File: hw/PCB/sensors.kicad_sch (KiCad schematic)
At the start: 1 part, among them U6 RM3100

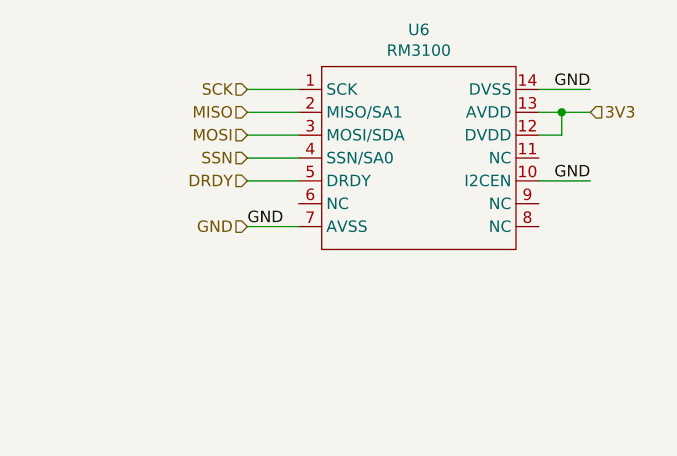
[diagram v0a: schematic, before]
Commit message: Modified the design of the femto-satellite. Now it is smaller an it has a temperature sensor to calibrate the magnetometer.
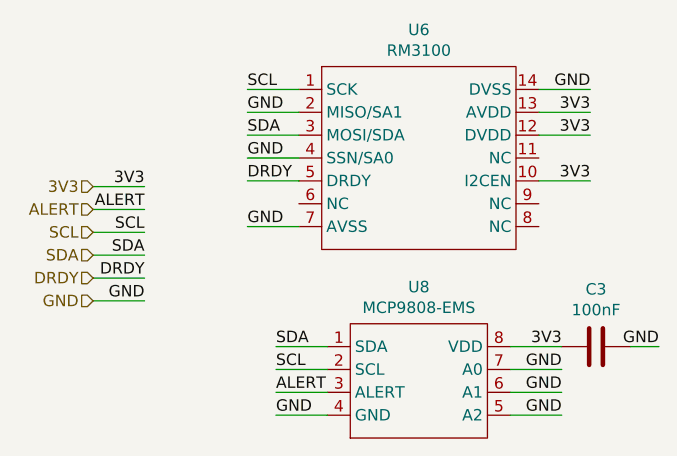
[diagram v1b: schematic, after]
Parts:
- added C3: 100nF, Capacitor_SMD:C_0603_1608Metric_Pad1.05x0.95mm_HandSolder, symbol Device:C
- added U8: MCP9808-EMS, Package_SO:MSOP-8_3x3mm_P0.65mm, symbol Temperature:MCP9808-EMS
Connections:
- net MISO is gone; now on net GND: U6.2 (MISO/SA1)
- net SSN is gone; now on net GND: U6.4 (SSN/SA0)
- net 3V3: now also U6.10 (I2CEN), C3.1, U8.8 (VDD)
- net GND: now also C3.2, U8.4 (GND), U8.5 (A2), U8.6 (A1), U8.7 (A0); no longer U6.10 (I2CEN)
- net MOSI renamed SDA
- net SDA: now also U8.1 (SDA)
- net SCK renamed SCL
- net SCL: now also U8.2 (SCL)
- new net ALERT: U8.3 (ALERT)
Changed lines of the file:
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@@
 (kicad_sch (version 20200512) (host eeschema "5.99.0-unknown-57e35c9~88~ubuntu19.10.1")
-  (page 1 7)
+  (page 5 6)
   (paper "A4")
-  (junction (at 159.385 86.995))
+  (wire (pts (xy 107.315 95.25) (xy 113.03 95.25))
+    (stroke (width 0) (type solid) (color 0 0 0 0))
+  )
+  (wire (pts (xy 107.315 97.79) (xy 113.03 97.79))
+    (stroke (width 0) (type solid) (color 0 0 0 0))
+  )
+  (wire (pts (xy 107.315 100.33) (xy 113.03 100.33))
+    (stroke (width 0) (type solid) (color 0 0 0 0))
+  )
+  (wire (pts (xy 107.315 102.87) (xy 113.03 102.87))
+    (stroke (width 0) (type solid) (color 0 0 0 0))
+  )
+  (wire (pts (xy 107.315 105.41) (xy 113.03 105.41))
+    (stroke (width 0) (type solid) (color 0 0 0 0))
+  )
+  (wire (pts (xy 107.315 107.95) (xy 113.03 107.95))
+    (stroke (width 0) (type solid) (color 0 0 0 0))
+  )
   (wire (pts (xy 124.46 84.455) (xy 130.175 84.455))
     (stroke (width 0) (type solid) (color 0 0 0 0))
@@
     (stroke (width 0) (type solid) (color 0 0 0 0))
   )
+  (wire (pts (xy 127.635 113.03) (xy 133.35 113.03))
+    (stroke (width 0) (type solid) (color 0 0 0 0))
+  )
+  (wire (pts (xy 127.635 115.57) (xy 133.35 115.57))
+    (stroke (width 0) (type solid) (color 0 0 0 0))
+  )
+  (wire (pts (xy 127.635 118.11) (xy 133.35 118.11))
+    (stroke (width 0) (type solid) (color 0 0 0 0))
+  )
+  (wire (pts (xy 127.635 120.65) (xy 133.35 120.65))
+    (stroke (width 0) (type solid) (color 0 0 0 0))
+  )
+  (wire (pts (xy 153.67 113.03) (xy 159.385 113.03))
+    (stroke (width 0) (type solid) (color 0 0 0 0))
+  )
+  (wire (pts (xy 153.67 115.57) (xy 159.385 115.57))
+    (stroke (width 0) (type solid) (color 0 0 0 0))
+  )
+  (wire (pts (xy 153.67 118.11) (xy 159.385 118.11))
+    (stroke (width 0) (type solid) (color 0 0 0 0))
+  )
+  (wire (pts (xy 153.67 120.65) (xy 159.385 120.65))
+    (stroke (width 0) (type solid) (color 0 0 0 0))
+  )
   (wire (pts (xy 156.845 84.455) (xy 162.56 84.455))
     (stroke (width 0) (type solid) (color 0 0 0 0))
   )
-  (wire (pts (xy 156.845 86.995) (xy 159.385 86.995))
+  (wire (pts (xy 156.845 86.995) (xy 162.56 86.995))
     (stroke (width 0) (type solid) (color 0 0 0 0))
   )
-  (wire (pts (xy 156.845 89.535) (xy 159.385 89.535))
+  (wire (pts (xy 156.845 89.535) (xy 162.56 89.535))
     (stroke (width 0) (type solid) (color 0 0 0 0))
   )
@@
     (stroke (width 0) (type solid) (color 0 0 0 0))
   )
-  (wire (pts (xy 159.385 86.995) (xy 162.56 86.995))
+  (wire (pts (xy 167.005 113.03) (xy 170.18 113.03))
     (stroke (width 0) (type solid) (color 0 0 0 0))
   )
-  (wire (pts (xy 159.385 89.535) (xy 159.385 86.995))
-    (stroke (width 0) (type solid) (color 0 0 0 0))
+  (label "3V3" (at 113.03 95.25 180)
+    (effects (font (size 1.27 1.27)) (justify right bottom))
+  )
+  (label "ALERT" (at 113.03 97.79 180)
+    (effects (font (size 1.27 1.27)) (justify right bottom))
+  )
+  (label "SCL" (at 113.03 100.33 180)
+    (effects (font (size 1.27 1.27)) (justify right bottom))
+  )
+  (label "SDA" (at 113.03 102.87 180)
+    (effects (font (size 1.27 1.27)) (justify right bottom))
+  )
+  (label "DRDY" (at 113.03 105.41 180)
+    (effects (font (size 1.27 1.27)) (justify right bottom))
+  )
+  (label "GND" (at 113.03 107.95 180)
+    (effects (font (size 1.27 1.27)) (justify right bottom))
+  )
+  (label "SCL" (at 124.46 84.455 0)
+    (effects (font (size 1.27 1.27)) (justify left bottom))
+  )
+  (label "GND" (at 124.46 86.995 0)
+    (effects (font (size 1.27 1.27)) (justify left bottom))
+  )
+  (label "SDA" (at 124.46 89.535 0)
+    (effects (font (size 1.27 1.27)) (justify left bottom))
+  )
+  (label "GND" (at 124.46 92.075 0)
+    (effects (font (size 1.27 1.27)) (justify left bottom))
+  )
+  (label "DRDY" (at 124.46 94.615 0)
+    (effects (font (size 1.27 1.27)) (justify left bottom))
   )
   (label "GND" (at 124.46 99.695 0)
     (effects (font (size 1.27 1.27)) (justify left bottom))
   )
+  (label "SDA" (at 127.635 113.03 0)
+    (effects (font (size 1.27 1.27)) (justify left bottom))
+  )
+  (label "SCL" (at 127.635 115.57 0)
+    (effects (font (size 1.27 1.27)) (justify left bottom))
+  )
+  (label "ALERT" (at 127.635 118.11 0)
+    (effects (font (size 1.27 1.27)) (justify left bottom))
+  )
+  (label "GND" (at 127.635 120.65 0)
+    (effects (font (size 1.27 1.27)) (justify left bottom))
+  )
+  (label "3V3" (at 159.385 113.03 180)
+    (effects (font (size 1.27 1.27)) (justify right bottom))
+  )
+  (label "GND" (at 159.385 115.57 180)
+    (effects (font (size 1.27 1.27)) (justify right bottom))
+  )
+  (label "GND" (at 159.385 118.11 180)
+    (effects (font (size 1.27 1.27)) (justify right bottom))
+  )
+  (label "GND" (at 159.385 120.65 180)
+    (effects (font (size 1.27 1.27)) (justify right bottom))
+  )
   (label "GND" (at 162.56 84.455 180)
     (effects (font (size 1.27 1.27)) (justify right bottom))
   )
-  (label "GND" (at 162.56 94.615 180)
+  (label "3V3" (at 162.56 86.995 180)
     (effects (font (size 1.27 1.27)) (justify right bottom))
   )
-  (hierarchical_label "SCK" (shape input) (at 124.46 84.455 180)
+  (label "3V3" (at 162.56 89.535 180)
+    (effects (font (size 1.27 1.27)) (justify right bottom))
+  )
+  (label "3V3" (at 162.56 94.615 180)
+    (effects (font (size 1.27 1.27)) (justify right bottom))
+  )
+  (label "GND" (at 170.18 113.03 180)
+    (effects (font (size 1.27 1.27)) (justify right bottom))
+  )
+  (hierarchical_label "3V3" (shape input) (at 107.315 95.25 180)
     (effects (font (size 1.27 1.27)) (justify right))
   )
-  (hierarchical_label "MISO" (shape input) (at 124.46 86.995 180)
+  (hierarchical_label "ALERT" (shape input) (at 107.315 97.79 180)
     (effects (font (size 1.27 1.27)) (justify right))
   )
-  (hierarchical_label "MOSI" (shape input) (at 124.46 89.535 180)
+  (hierarchical_label "SCL" (shape input) (at 107.315 100.33 180)
     (effects (font (size 1.27 1.27)) (justify right))
   )
-  (hierarchical_label "SSN" (shape input) (at 124.46 92.075 180)
+  (hierarchical_label "SDA" (shape input) (at 107.315 102.87 180)
     (effects (font (size 1.27 1.27)) (justify right))
   )
-  (hierarchical_label "DRDY" (shape input) (at 124.46 94.615 180)
+  (hierarchical_label "DRDY" (shape input) (at 107.315 105.41 180)
     (effects (font (size 1.27 1.27)) (justify right))
   )
-  (hierarchical_label "GND" (shape input) (at 124.46 99.695 180)
+  (hierarchical_label "GND" (shape input) (at 107.315 107.95 180)
     (effects (font (size 1.27 1.27)) (justify right))
   )
-  (hierarchical_label "3V3" (shape input) (at 162.56 86.995 0)
-    (effects (font (size 1.27 1.27)) (justify left))
+  (symbol (lib_id "Device:C") (at 163.195 113.03 90) (unit 1)
+    (property "Reference" "C3" (id 0) (at 163.195 106.6608 90))
+    (property "Value" "100nF" (id 1) (at 163.195 108.9595 90))
+    (property "Footprint" "Capacitor_SMD:C_0603_1608Metric_Pad1.05x0.95mm_HandSolder" (id 2) (at 167.005 112.0648 0)
+      (effects (font (size 1.27 1.27)) hide)
+    )
+    (property "Datasheet" "~" (id 3) (at 163.195 113.03 0)
+      (effects (font (size 1.27 1.27)) hide)
+    )
+  )
+  (symbol (lib_id "Temperature:MCP9808-EMS") (at 143.51 116.84 0) (unit 1)
+    (property "Reference" "U8" (id 0) (at 143.51 106.4065 0))
+    (property "Value" "MCP9808-EMS" (id 1) (at 143.51 108.7052 0))
+    (property "Footprint" "Package_SO:MSOP-8_3x3mm_P0.65mm" (id 2) (at 143.51 109.22 0)
+      (effects (font (size 1.27 1.27)) hide)
+    )
+    (property "Datasheet" "" (id 3) (at 143.51 109.22 0)
+      (effects (font (size 1.27 1.27)) hide)
+    )
   )
   (symbol (lib_id "rm3100:RM3100") (at 144.145 92.075 0) (unit 1)
